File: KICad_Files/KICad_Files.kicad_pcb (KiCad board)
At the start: 2 copper layers, 30 x 34 mm, 42 parts, among them J1 Conn_01x03_MountingPin, J2 Conn_01x03_MountingPin, J3 Conn_01x03_MountingPin, J4 USB_C_Receptacle_USB2.0_14P, J5 Conn_01x06, J6 Conn_01x06, J7 Conn_01x03_Pin, J8 Conn_01x03_Pin, SW1 Reset, SW2 Boot, U1 TPP361061-T6TR, U2 USBLC6-2SC6, U3 ESP32-C3

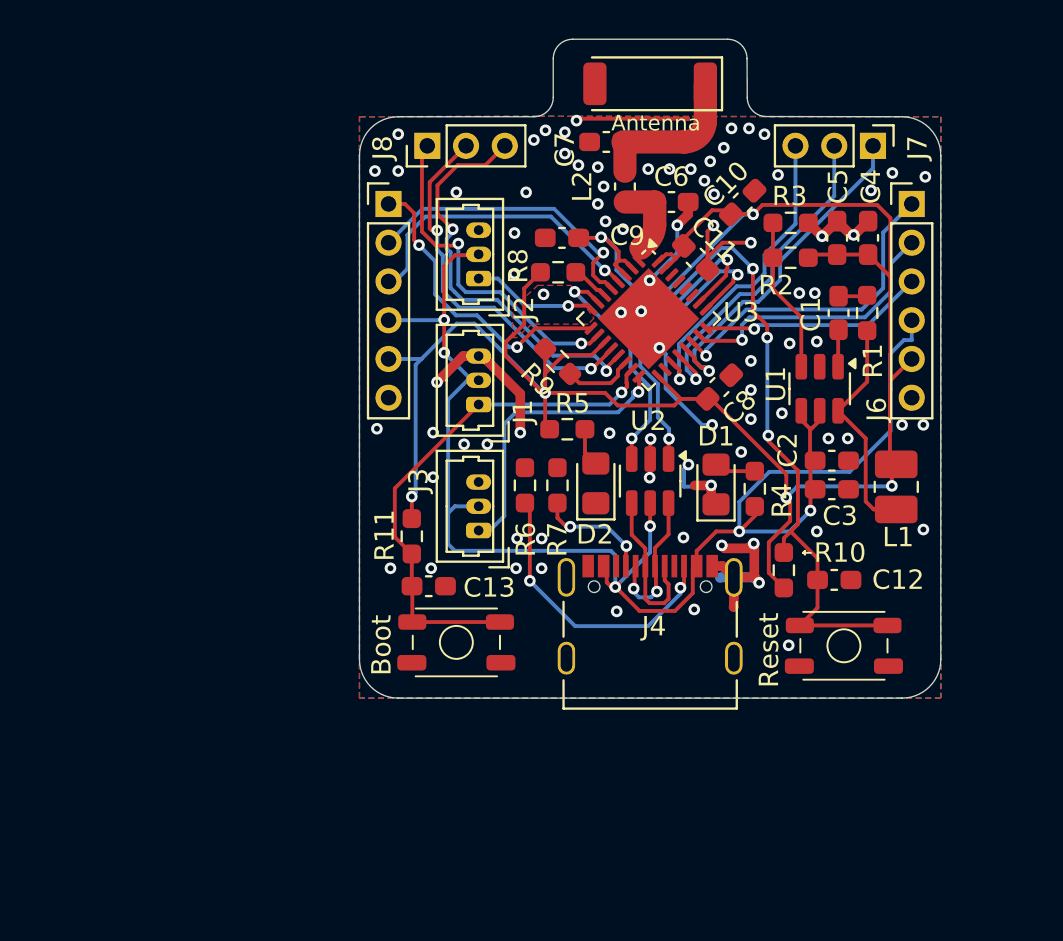
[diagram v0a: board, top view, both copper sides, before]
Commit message: Complete rework of the PCB routing
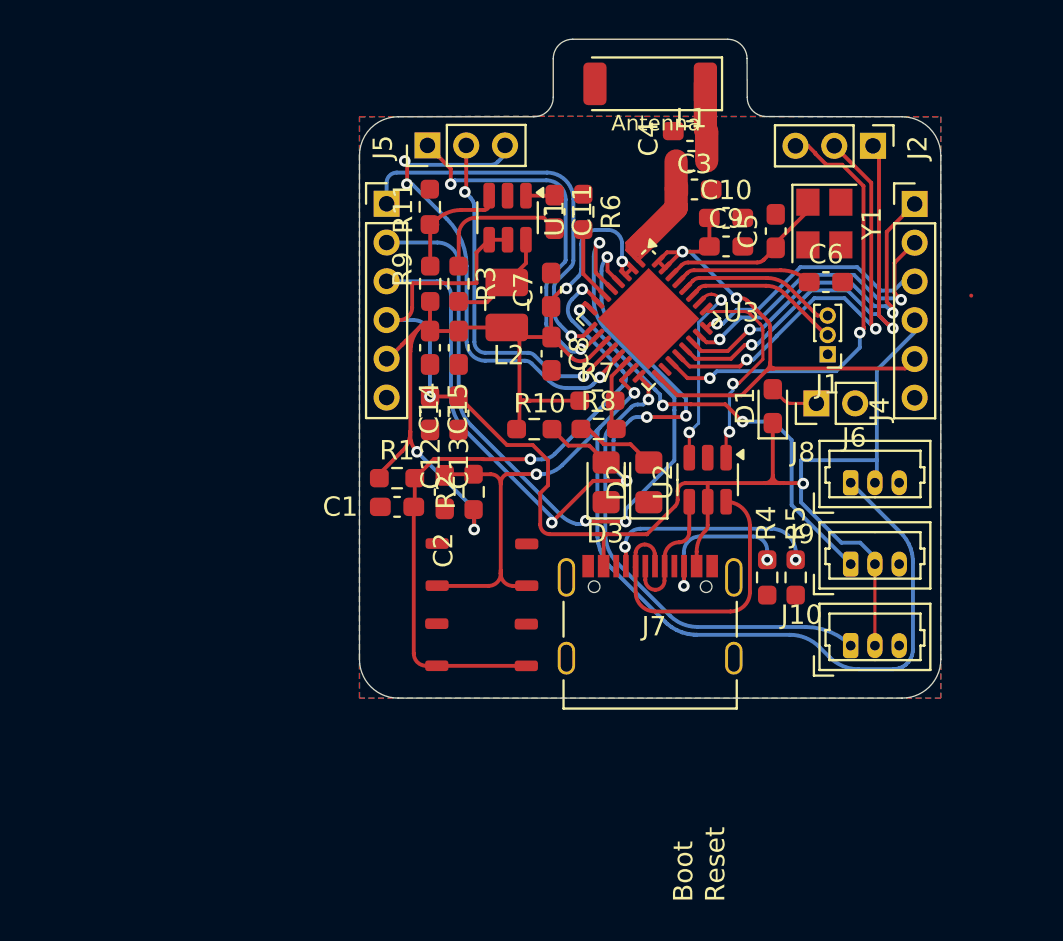
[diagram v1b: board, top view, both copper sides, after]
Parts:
- removed the C11 at (109.2, 91.7)
- removed the R10 at (113.7, 107.8)
- removed the R11 at (94.5, 106.1)
- removed the R4 at (112.2, 103.6)
- removed the R9 at (102.0, 97.0)
- added C5: 26pF, Capacitor_SMD:C_0603_1608Metric_Pad1.08x0.95mm_HandSolder, F.Cu at (113.3, 90.3)
- added C6: 26pF, Capacitor_SMD:C_0603_1608Metric_Pad1.08x0.95mm_HandSolder, F.Cu at (115.9, 92.9)
- added C7: 100 nF, Capacitor_SMD:C_0603_1608Metric_Pad1.08x0.95mm_HandSolder, F.Cu at (101.7, 93.3)
- added D2: LED, LED_SMD:LED_0805_2012Metric_Pad1.15x1.40mm_HandSolder, F.Cu at (106.7, 103.3)
- added J1: Conn_01x03_Pin, Connector_PinHeader_1.00mm:PinHeader_1x03_P1.00mm_Vertical, F.Cu at (116.0, 96.7)
- added J6: Conn_01x02_Pin, Connector_PinHeader_2.00mm:PinHeader_1x02_P2.00mm_Vertical, F.Cu at (115.4, 99.2)
- added R2: 10k, Resistor_SMD:R_0603_1608Metric_Pad0.98x0.95mm_HandSolder, F.Cu at (97.7, 103.8)
- added R3: 0 Ω, Resistor_SMD:R_0603_1608Metric_Pad0.98x0.95mm_HandSolder, F.Cu at (96.9, 93.0)
- added R6: 10kΩ, Resistor_SMD:R_0603_1608Metric_Pad0.98x0.95mm_HandSolder, F.Cu at (103.4, 89.3)
- added R7: 10kΩ, Resistor_SMD:R_0603_1608Metric_Pad0.98x0.95mm_HandSolder, F.Cu at (104.1, 99.1)
- added Y1: 40.0MHz, Crystal:Crystal_SMD_3225-4Pin_3.2x2.5mm, F.Cu at (115.8, 89.9)
- C10: value 100 nF -> 10 uF
- D1: value LED -> D; footprint LED_SMD:LED_0805_2012Metric_Pad1.15x1.40mm_HandSolder -> Diode_SMD:D_0603_1608Metric_Pad1.05x0.95mm_HandSolder
- R1: value 0 Ω -> 10k
- R8: value 10kΩ -> 560Ω
- SW1, SW2: footprint Micro_button:Micro_button -> Micro_button:RKB2SJK250SMTR LFS
- moved R1 25.7 mm to (93.7, 103.1), turned to 0 degrees
- moved J9 24.2 mm to (117.2, 107.5), turned to 0 degrees
- moved C14 23.3 mm to (95.4, 96.3), turned to 90 degrees
- moved C1 22.9 mm to (93.7, 104.5), turned to 180 degrees
- moved L2 22.2 mm to (99.4, 94.1)
- moved C12 20.9 mm to (95.4, 99.7), turned to 90 degrees
- moved C15 20.3 mm to (96.9, 96.3), turned to 90 degrees
- moved J10 20.1 mm to (117.2, 111.7), turned to 0 degrees
- moved C13 19.7 mm to (96.9, 99.7), turned to 90 degrees
- moved J8 19.6 mm to (117.2, 103.3), turned to 0 degrees
- moved SW1 18.7 mm to (98.1, 111.7)
- moved R9 18.6 mm to (95.5, 93.0), turned to 90 degrees
- moved R11 18.6 mm to (95.4, 89.1), turned to -90 degrees
- moved U1 18.4 mm to (99.4, 89.6)
- moved C11 15.6 mm to (101.9, 89.3), turned to -90 degrees
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- renumbered C12 to C1, C1 to C11, C2 to C12, C3 to C13, C4 to C14, C5 to C15, C13 to C2, C6 to C3, C7 to C4, D2 to D3, J3 to J10, J7 to J2, J5 to J3, J6 to J4, J8 to J5, J4 to J7, J1 to J8, J2 to J9, L2 to L1, L1 to L2, R5 to R10, R3 to R11, R6 to R4, R7 to R5, R2 to R9
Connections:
- C1 pad 1: Net-(U3-CHIP_EN) -> /CHIP_EN
- C11 pad 2: Net-(C1-Pad2) -> Net-(C11-Pad2)
- D1 pad 1: GND -> +5V
- R1 pad 1: Net-(C1-Pad2) -> +3.3V
- R1 pad 2: Net-(U1-SW) -> /CHIP_EN
- R8 pad 1: +3.3V -> Net-(D2-A)
- R8 pad 2: Net-(U3-GPIO2) -> Net-(U3-GPIO8)
- SW1 pad 2: Net-(U3-CHIP_EN) -> /CHIP_EN
- U3 pad 27: unconnected-(U3-U0RXD-Pad27) -> /U0RXD
- U3 pad 28: unconnected-(U3-U0TXD-Pad28) -> /U0TXD
- U3 pad 29: unconnected-(U3-XTAL_N-Pad29) -> /XTAL_N
- U3 pad 30: unconnected-(U3-XTAL_P-Pad30) -> /XTAL_P
- U3 pad 7: Net-(U3-CHIP_EN) -> /CHIP_EN
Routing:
- net GND: track 52.2 -> 2.10 mm, vias 83 -> 0
- net Net-(U3-CHIP_EN): track 40.3 -> 0.00 mm, vias 4 -> 0
- net /CHIP_EN: track 0.00 -> 35.5 mm, vias 0 -> 2
- net /LED3: track 27.0 -> 60.0 mm, vias 1 -> 2
- net +3.3V: track 116.2 -> 83.4 mm
- net /GPIO 1: track 15.5 -> 43.0 mm, vias 1 -> 3
- net /GPIO 0: track 15.7 -> 41.8 mm, vias 1 -> 5
- net /LED2: track 6.46 -> 22.9 mm, vias 1 -> 3
- net /LED1: track 15.0 -> 24.7 mm
- net /XTAL_P: track 0.00 -> 9.31 mm
- net /U0TXD: track 0.00 -> 8.27 mm
- net Net-(J7-D--PadA7): track 7.71 -> 15.9 mm, vias 2 -> 0
- net /U0RXD: track 0.00 -> 8.16 mm
- net /XTAL_N: track 0.00 -> 7.58 mm
- net /GPIO 12: track 16.0 -> 23.5 mm, vias 1 -> 2
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
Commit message: Fixed errors and silkscreen overlapping
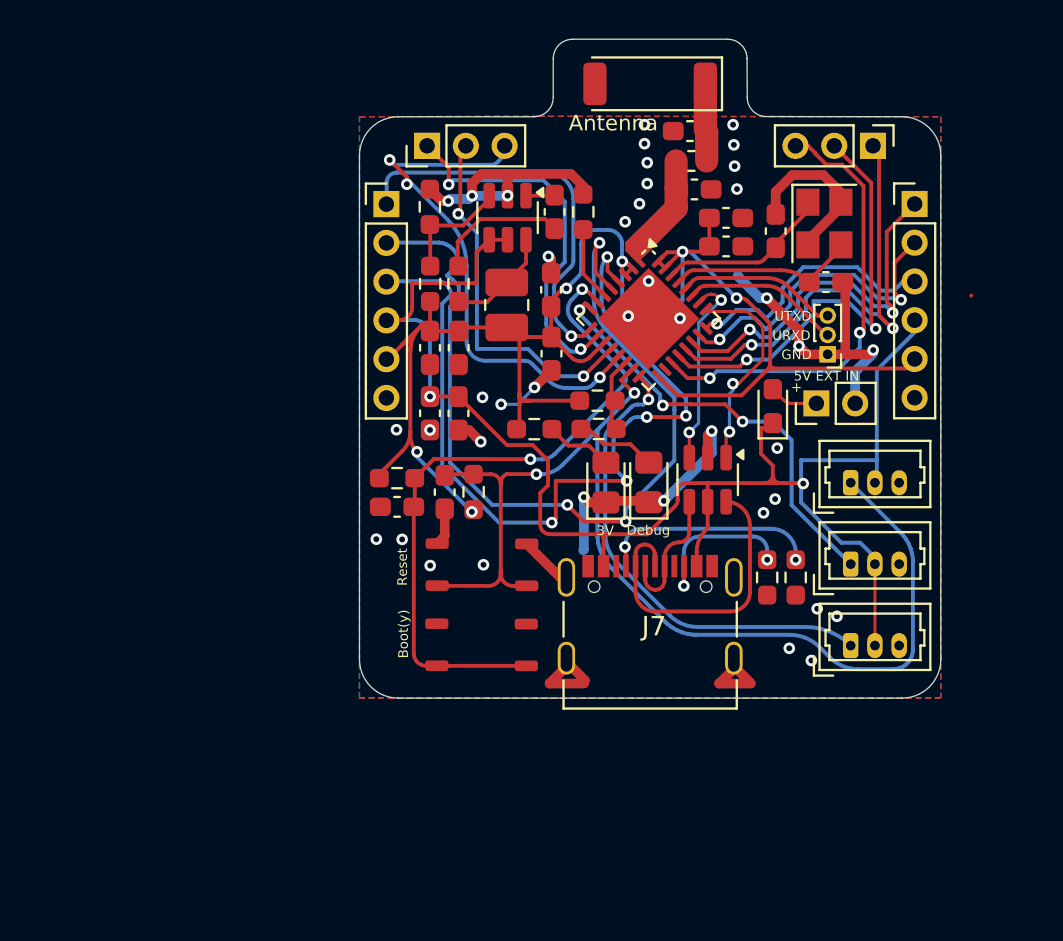
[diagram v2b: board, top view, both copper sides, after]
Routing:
- net GND: track 2.10 -> 74.1 mm, vias 0 -> 40
- net +3.3V: track 83.4 -> 89.1 mm
- net /GPIO 0: track 41.8 -> 45.0 mm
- net /GPIO 1: track 43.0 -> 45.8 mm
- net /XTAL_N: track 7.58 -> 10.2 mm
- net /GPIO 7: track 26.2 -> 27.4 mm
- net /GPIO 16: track 16.1 -> 17.0 mm
- net +5V: track 78.3 -> 79.1 mm
- net VFB: track 7.05 -> 6.26 mm
- net /GPIO 17: track 12.8 -> 13.5 mm
- net /GPIO 15: track 19.0 -> 19.7 mm
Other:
- board text added: "+"
- board text added: "3V"
- board text added: "5V EXT IN"
- board text added: "Boot(y)"
- board text added: "Debug"
- board text added: "ESP32-C3 LED-Devboard Made by Kideya Date: 02.2025 | Rev.2"
- board text added: "GPIO0"
- board text added: "GPIO1"
- board text added: "GPIO10"
- board text added: "GPIO12"
- board text added: "GPIO13"
- board text added: "GPIO14"
- board text added: "GPIO15"
- board text added: "GPIO16"
- board text added: "GPIO17"
- board text added: "GPIO3"
- board text added: "GPIO4"
- board text added: "GPIO5"
- board text added: "GPIO6"
- board text added: "GPIO7"
- board text added: "GPIO9"
- board text added: "URXD"
- board text added: "UTXD"
- board text removed: "Boot"
- board text removed: "ESP32-C3 LED-Devboard Made by Kideya Date: 01.2025 | Rev.1"
- board text removed: "GPIO0/4"
- board text removed: "GPIO1/5"
- board text removed: "GPIO10/16"
- board text removed: "GPIO12/19"
- board text removed: "GPIO13/20"
- board text removed: "GPIO14/21"
- board text removed: "GPIO15/22"
- board text removed: "GPIO16/23"
- board text removed: "GPIO17/24"
- board text removed: "GPIO3/8"
- board text removed: "GPIO4/9"
- board text removed: "GPIO5/10"
- board text removed: "GPIO6/12"
- board text removed: "GPIO7/13"
- board text removed: "GPIO9/15"

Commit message: removed some loose tracks
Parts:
- J7: value USB_C_Receptacle_USB2.0_14P -> USB_C_Receptacle_USB2.0_16P
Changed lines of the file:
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@@
 			(at 0.2 0.6 0)
 			(layer "F.SilkS")
+			(hide yes)
 			(effects
 				(font
@@
 			)
 		)
-		(property "Value" "USB_C_Receptacle_USB2.0_14P"
+		(property "Value" "USB_C_Receptacle_USB2.0_16P"
 			(at 0 6.24 0)
 			(layer "F.Fab")
@@
 			(unlocked yes)
 			(layer "F.Fab")
-			(hide yes)
 			(effects
 				(font
@@
 	)
 	(segment
-		(start 100.238599 99.050001)
-		(end 100.60116 99.050001)
-		(width 0.2)
-		(layer "F.Cu")
-		(net 3)
-	)
-	(segment
 		(start 104.45855 96.023374)
 		(end 104.45855 96.031452)
@@
 		(width 0.2)
 		(layer "F.Cu")
-		(net 3)
-	)
-	(segment
-		(start 94.456669 101.140001)
-		(end 94.459474 101.140001)
-		(width 0.2)
-		(layer "F.Cu")

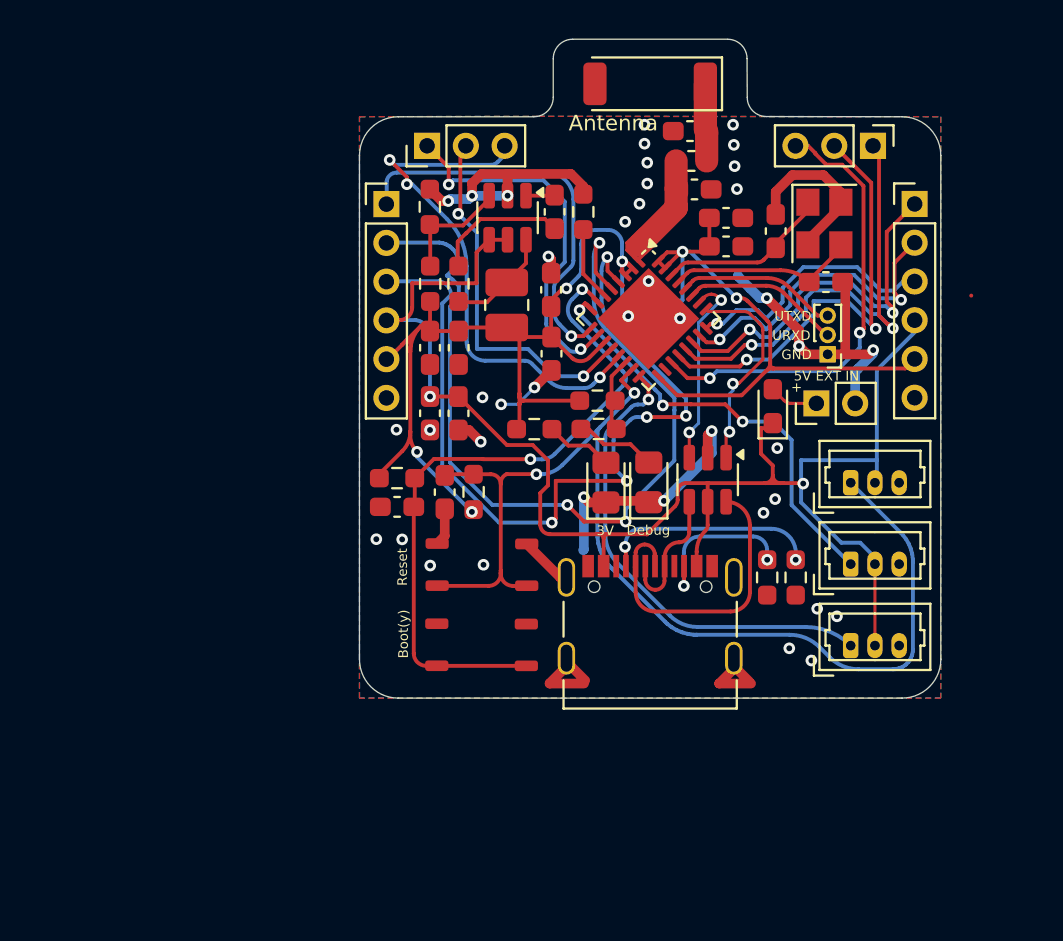
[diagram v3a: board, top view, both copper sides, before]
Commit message: Redesign Add 24V buck converter
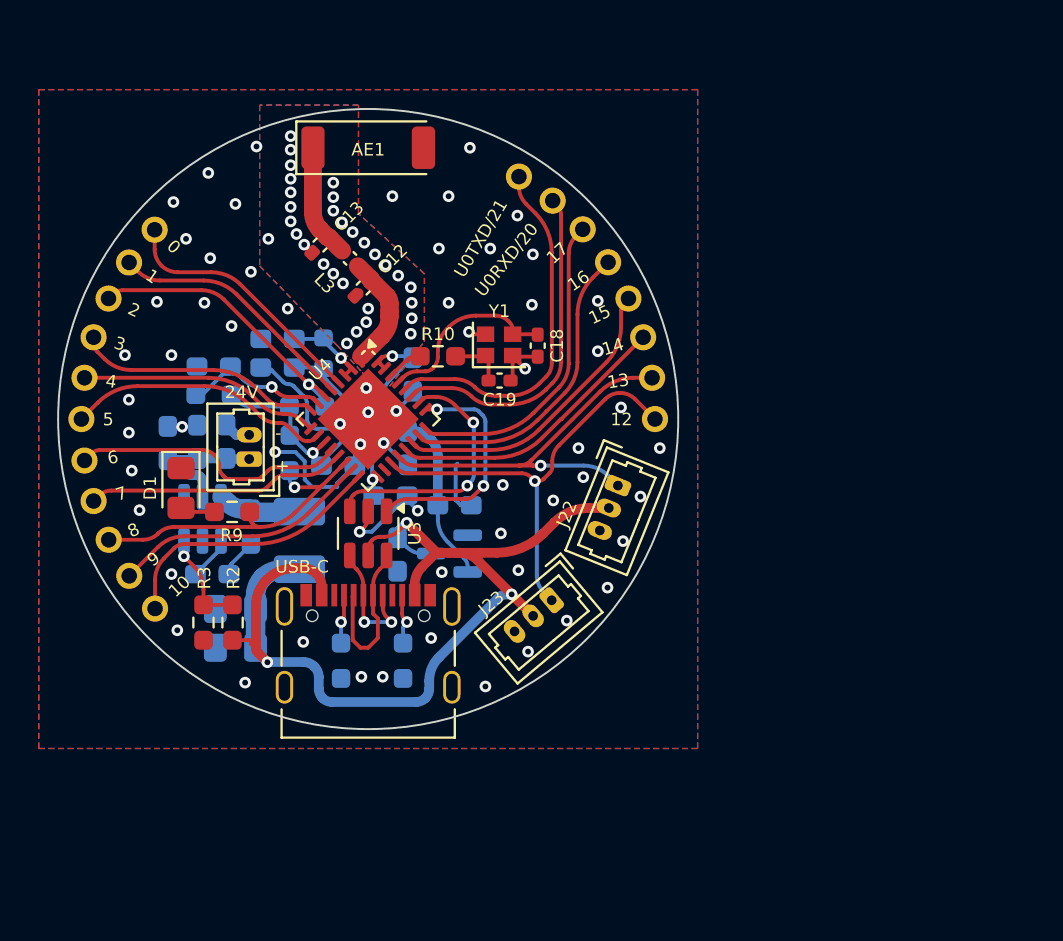
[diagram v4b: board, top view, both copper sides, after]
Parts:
- removed D2, D3: LED, LED_SMD:LED_0805_2012Metric_Pad1.15x1.40mm_HandSolder
- removed R11: 15kΩ, Resistor_SMD:R_0603_1608Metric_Pad0.98x0.95mm_HandSolder
- removed SW1: Reset, Micro_button:RKB2SJK250SMTR LFS
- removed SW2: Boot, Micro_button:RKB2SJK250SMTR LFS
- added C16: 100 nF, Capacitor_SMD:C_0603_1608Metric_Pad1.08x0.95mm_HandSolder, B.Cu at (90.7, 102.4)
- added C17: 10 uF, Capacitor_SMD:C_0603_1608Metric_Pad1.08x0.95mm_HandSolder, B.Cu at (94.3, 101.5)
- added C18: 10pF, Capacitor_SMD:C_0402_1005Metric_Pad0.74x0.62mm_HandSolder, F.Cu at (101.0, 96.2)
- added C19: 10pF, Capacitor_SMD:C_0402_1005Metric_Pad0.74x0.62mm_HandSolder, F.Cu at (99.0, 98.0)
- added J11: Conn_01x06, extraFootprints:01_P2.00mm, F.Cu at (105.7, 93.8)
- added J12: USB_C_Receptacle_USB2.0_16P, Connector_USB:USB_C_Receptacle_Palconn_UTC16-G, F.Cu at (92.2, 111.6)
- added J13: Conn_01x06, extraFootprints:01_P2.00mm, F.Cu at (77.5, 100.0)
- added J14: Conn_01x06, extraFootprints:01_P2.00mm, F.Cu at (106.4, 95.8)
- added J15: Conn_01x06, extraFootprints:01_P2.00mm, F.Cu at (77.6, 97.9)
- added J16: Conn_01x06, extraFootprints:01_P2.00mm, F.Cu at (106.9, 97.9)
- added J17: Conn_01x06, extraFootprints:01_P2.00mm, F.Cu at (78.1, 95.8)
- added J18: Conn_01x06, extraFootprints:01_P2.00mm, F.Cu at (107.0, 100.0)
- added J19: Conn_01x06, extraFootprints:01_P2.00mm, F.Cu at (78.8, 93.8)
- added J20: Conn_01x06, extraFootprints:01_P2.00mm, F.Cu at (79.9, 91.9)
- added J21: Conn_01x06, extraFootprints:01_P2.00mm, F.Cu at (81.2, 90.2)
- added J22: Conn_01x03_MountingPin, Connector_Molex:Molex_PicoBlade_53047-0310_1x03_P1.25mm_Vertical, F.Cu at (105.1, 103.4)
- added J23: Conn_01x03_MountingPin, Connector_Molex:Molex_PicoBlade_53047-0310_1x03_P1.25mm_Vertical, F.Cu at (101.7, 109.4)
- added L3: 6n2, Inductor_SMD:L_0402_1005Metric_Pad0.77x0.64mm_HandSolder, F.Cu at (91.3, 91.7)
- added U4: ESP32-C3, Package_DFN_QFN:QFN-32-1EP_5x5mm_P0.5mm_EP3.7x3.7mm, F.Cu at (92.2, 100.0)
- C1: value 100 nF -> 100n; moved to B.Cu
- C10: value 10 uF -> 100n; moved to B.Cu
- C11, C2, C9: value 100 nF -> 1u; moved to B.Cu
- C12: value 10 uF -> 1p5; footprint Capacitor_SMD:C_0603_1608Metric_Pad1.08x0.95mm_HandSolder -> Capacitor_SMD:C_0402_1005Metric_Pad0.74x0.62mm_HandSolder
- C13: value 100 nF -> 1p5; footprint Capacitor_SMD:C_0603_1608Metric_Pad1.08x0.95mm_HandSolder -> Capacitor_SMD:C_0402_1005Metric_Pad0.74x0.62mm_HandSolder
- C14, C15: value 22 μF -> 100 nF; moved to B.Cu
- C3: value 3p3 -> 1u; moved to B.Cu
- C4: value 3p3 -> 10u 35V; moved to B.Cu
- C5: value 26pF -> 10u 35V; moved to B.Cu
- C6: value 26pF -> 100n 35V; moved to B.Cu
- C7, C8: value 100 nF -> 22u; footprint Capacitor_SMD:C_0603_1608Metric_Pad1.08x0.95mm_HandSolder -> Capacitor_SMD:C_0805_2012Metric_Pad1.18x1.45mm_HandSolder; moved to B.Cu
- D1: value D -> LED; footprint Diode_SMD:D_0603_1608Metric_Pad1.05x0.95mm_HandSolder -> LED_SMD:LED_0805_2012Metric_Pad1.15x1.40mm_HandSolder
- J1: value Conn_01x03_Pin -> Power Input; footprint Connector_PinHeader_1.00mm:PinHeader_1x03_P1.00mm_Vertical -> Connector_Molex:Molex_PicoBlade_53047-0210_1x02_P1.25mm_Vertical
- J10, J8, J9: value Conn_01x03_MountingPin -> Conn_01x06; footprint Connector_Molex:Molex_PicoBlade_53047-0310_1x03_P1.25mm_Vertical -> extraFootprints:01_P2.00mm
- J2, J5: value Conn_01x03_Pin -> Conn_01x06; footprint Connector_PinHeader_2.00mm:PinHeader_1x03_P2.00mm_Vertical -> extraFootprints:01_P2.00mm
- J3, J4: footprint Connector_PinHeader_2.00mm:PinHeader_1x06_P2.00mm_Vertical -> extraFootprints:01_P2.00mm
- J6: value Conn_01x02_Pin -> Conn_01x06; footprint Connector_PinHeader_2.00mm:PinHeader_1x02_P2.00mm_Vertical -> extraFootprints:01_P2.00mm
- J7: value USB_C_Receptacle_USB2.0_16P -> Conn_01x06; footprint Connector_USB:USB_C_Receptacle_Palconn_UTC16-G -> extraFootprints:01_P2.00mm
- L1: value 2n2 -> 10u (1276AS-H-100M=P2); footprint Inductor_SMD:L_0603_1608Metric -> Inductor_SMD:L_1210_3225Metric_Pad1.42x2.65mm_HandSolder; moved to B.Cu
- L2: value 10 uH -> 2n2; footprint Inductor_SMD:L_1008_2520Metric_Pad1.43x2.20mm_HandSolder -> Inductor_SMD:L_0603_1608Metric; moved to B.Cu
- R1: value 10k -> 0R; moved to B.Cu
- R10: value 560Ω -> 10R
- R2: value 10k -> 11k
- R3: value 0 Ω -> 1k5
- R4: value 5.1 kΩ -> 10k; moved to B.Cu
- R5: value 5.1 kΩ -> 10kΩ; moved to B.Cu
- R6: moved to B.Cu
- R7: value 10kΩ -> 5k1; moved to B.Cu
- R8: value 560Ω -> 5k1; moved to B.Cu
- R9: value 68kΩ -> 560Ω
- U1: value TPP361061-T6TR -> MCP1703Ax-330xxTT; footprint Package_TO_SOT_SMD:SOT-23-6 -> Package_TO_SOT_SMD:SOT-23; moved to B.Cu
- U2: value USBLC6-2SC6 -> TPP361061-T6TR; moved to B.Cu
- U3: value ESP32-C3 -> USBLC6-2SC6; footprint Package_DFN_QFN:QFN-32-1EP_5x5mm_P0.5mm_EP3.7x3.7mm -> Package_TO_SOT_SMD:SOT-23-6
- Y1: value 40.0MHz -> E9X400081G08; footprint Crystal:Crystal_SMD_3225-4Pin_3.2x2.5mm -> Crystal:Crystal_SMD_2016-4Pin_2.0x1.6mm
- moved J4 44.8 mm to (79.9, 108.1), turned to 34 degrees
- moved J2 44.1 mm to (81.2, 109.8), turned to 42.5 degrees
- moved J10 40.7 mm to (77.6, 102.1), turned to 8.5 degrees
- moved J8 39.1 mm to (78.1, 104.2), turned to 17 degrees
- moved J6 37.2 mm to (78.9, 106.2), turned to 25.5 degrees
- moved C6 35.0 mm to (81.9, 101.2), turned to -90 degrees
- moved C5 31.8 mm to (83.4, 101.2), turned to -90 degrees
- moved D1 30.8 mm to (82.6, 103.6), turned to -90 degrees
- moved J1 30.3 mm to (86.1, 102.1), turned to 90 degrees
- moved R4 30.1 mm to (84.3, 98.8), turned to 180 degrees
- moved C4 28.8 mm to (84.9, 101.2), turned to -90 degrees
- moved L1 28.2 mm to (88.7, 106.3), turned to 90 degrees
- moved C9 27.2 mm to (84.3, 97.3), turned to 180 degrees
- moved R5 26.7 mm to (89.1, 99.3), turned to 0 degrees
- moved U2 26.1 mm to (83.7, 105.2), turned to 90 degrees
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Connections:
- C1 pad 1: /CHIP_EN -> Net-(U2-VBST)
- C1 pad 2: GND -> Net-(C1-Pad2)
- C11 pad 1: Net-(U1-VBST) -> Net-(C11-Pad1)
- C11 pad 2: Net-(C11-Pad2) -> GND
- C12 pad 1: GND -> Net-(U4-LNA_IN)
- C12 pad 2: +5V -> GND
- C13 pad 1: GND -> Net-(AE1-FEED)
- C13 pad 2: +5V -> GND
- C14 pad 1: GND -> +3.3V
- C14 pad 2: +3.3V -> GND
- C15 pad 1: GND -> +3.3V
- C15 pad 2: +3.3V -> GND
- C2 pad 1: /LED3 -> +5V
- C3 pad 1: /Antenna -> +3.3V
- C4 pad 1: Net-(AE1-FEED) -> GND
- C4 pad 2: GND -> +24V
- C5 pad 1: /XTAL_P -> GND
- C5 pad 2: GND -> +24V
- C6 pad 1: /XTAL_N -> GND
- C6 pad 2: GND -> +24V
- C7 pad 1: +3.3V -> GND
- C7 pad 2: GND -> +5V
- C8 pad 1: +3.3V -> GND
- C8 pad 2: GND -> +5V
- C9 pad 1: +3.3V -> Net-(U4-CHIP_EN)
- D1 pad 1: +5V -> GND
- J1 pad 1: GND -> +24V
- J1 pad 2: /U0RXD -> GND
- J10 pad 1: /LED1 -> /GPIO 6
- J2 pad 1: /GPIO 14 -> /GPIO 10
- J3 pad 1: /GPIO 4 -> /U0TXD/GPIO 21
- J4 pad 1: /GPIO 15 -> /GPIO 9
- J5 pad 1: /GPIO 5 -> /U0RXD/GPIO 20
- J6 pad 1: Net-(D1-A) -> /GPIO 8
- J8 pad 1: /LED3 -> /GPIO 7
- J9 pad 1: /LED2 -> /GPIO 16
- L1 pad 1: /Antenna -> +5V
- L1 pad 2: Net-(AE1-FEED) -> Net-(U2-SW)
- L2 pad 2: Net-(U1-SW) -> Net-(C11-Pad1)
- R1 pad 1: +3.3V -> Net-(C1-Pad2)
- R1 pad 2: /CHIP_EN -> Net-(U2-SW)
- R10 pad 1: +3.3V -> Net-(U4-XTAL_P)
- R10 pad 2: Net-(D3-A) -> Net-(C19-Pad1)
- R2 pad 1: +3.3V -> +5V
- R2 pad 2: /LED3 -> Net-(U2-VFB)
- R3 pad 1: Net-(C11-Pad2) -> GND
- R3 pad 2: Net-(U1-SW) -> Net-(U2-VFB)
- R4 pad 1: GND -> +3.3V
- R4 pad 2: Net-(J7-CC2) -> Net-(U4-CHIP_EN)
- R5 pad 1: GND -> +3.3V
- R5 pad 2: Net-(J7-CC1) -> /GPIO 2
- R6 pad 1: GND -> /GPIO 8
- R6 pad 2: Net-(U3-GPIO2) -> +3.3V
- R7 pad 1: +3.3V -> GND
- R7 pad 2: Net-(U3-GPIO8) -> Net-(J12-CC2)
- R8 pad 1: Net-(D2-A) -> GND
- R8 pad 2: Net-(U3-GPIO8) -> Net-(J12-CC1)
- R9 pad 1: +3.3V -> Net-(D1-A)
- R9 pad 2: VFB -> /GPIO 8
- U1 pad 1: Net-(U1-VBST) -> GND
- U1 pad 2: GND -> +3.3V
- U1 pad 3: VFB -> +5V
- U2 pad 1: D- -> Net-(U2-VBST)
- U2 pad 3: D+ -> Net-(U2-VFB)
- U2 pad 4: Net-(J7-D+-PadA6) -> unconnected-(U2-EN-Pad4)
- U2 pad 5: +5V -> +24V
- U2 pad 6: Net-(J7-D--PadA7) -> Net-(U2-SW)
- U3 pad 1: /Antenna -> D-
- U3 pad 2: +3.3V -> GND
- U3 pad 3: +3.3V -> D+
- U3 pad 4: /GPIO 0 -> /D_Raw+
- U3 pad 5: /GPIO 1 -> +5V
- U3 pad 6: Net-(U3-GPIO2) -> /D_Raw-
- Y1 pad 1: /XTAL_P -> Net-(C19-Pad1)
- Y1 pad 3: /XTAL_N -> Net-(U4-XTAL_N)
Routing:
- net /LED3: track 60.0 -> 0.00 mm, vias 2 -> 0
- net +3.3V: track 88.7 -> 39.5 mm, vias 6 -> 3
- net GND: track 74.1 -> 30.8 mm, vias 40 -> 92
- net /CHIP_EN: track 35.5 -> 0.00 mm, vias 2 -> 0
- net /GPIO 1: track 45.8 -> 12.9 mm, vias 3 -> 0
- net /GPIO 0: track 45.0 -> 13.4 mm, vias 5 -> 0
- net /LED1: track 24.7 -> 0.00 mm, vias 1 -> 0
- net /LED2: track 22.9 -> 0.00 mm, vias 3 -> 0
- net +5V: track 79.1 -> 59.7 mm, vias 2 -> 3
- net /U0TXD/GPIO 21: track 0.00 -> 18.9 mm
- net /U0RXD/GPIO 20: track 0.00 -> 17.6 mm
- net /GPIO 8: track 0.00 -> 17.2 mm, vias 0 -> 1
- net Net-(J7-D--PadA7): track 15.9 -> 0.00 mm
- net /GPIO 2: track 0.00 -> 14.9 mm, vias 0 -> 1
- net /GPIO 10: track 0.00 -> 14.2 mm
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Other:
- board size 30 x 34 mm -> 32 x 32 mm
- board text added: "-"
- board text added: "0"
- board text added: "1"
- board text added: "10"
- board text added: "12"
- board text added: "13"
- board text added: "14"
- board text added: "15"
- board text added: "16"
- board text added: "17"
- board text added: "2"
- board text added: "24V"
- board text added: "3"
- board text added: "4"
- board text added: "5"
- board text added: "6"
- board text added: "7"
- board text added: "8"
- board text added: "9"
- board text added: "ESP32-C3 2025-04 by MG-5"
- board text added: "U0RXD/20"
- board text added: "U0TXD/21"
- board text added: "USB-C"
- board text removed: "3.3V"
- board text removed: "3V"
- board text removed: "5V"
- board text removed: "5V EXT IN"
- board text removed: "Antenna"
- board text removed: "Blind-Deer Studio"
- board text removed: "Boot(y)"
- board text removed: "Debug"
- board text removed: "ESP32-C3 LED-Devboard Made by Kideya Date: 02.2025 | Rev.2"
- board text removed: "GND"
- board text removed: "GPIO0"
- board text removed: "GPIO1"
- board text removed: "GPIO10"
- board text removed: "GPIO12"
- board text removed: "GPIO13"
- board text removed: "GPIO14"
- board text removed: "GPIO15"
- board text removed: "GPIO16"
- board text removed: "GPIO17"
- board text removed: "GPIO3"
- board text removed: "GPIO4"
- board text removed: "GPIO5"
- board text removed: "GPIO6"
- board text removed: "GPIO7"
- board text removed: "GPIO9"
- board text removed: "Github: Kideya/ESP32-C3-LED-Connector"
- board text removed: "Reset"
- board text removed: "URXD"
- board text removed: "UTXD"
